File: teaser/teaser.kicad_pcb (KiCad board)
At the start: 2 copper layers, 71 parts, among them J1 Programator, J2 AC_Plug, J3 OLED, J4 battery, Q1 MMBTA44, Q2 MMBTA44, Q3 MMBTA44, Q4 MMBTA44, Q6 AO3401A, SW1 Włancznik, SW2 SW_SPST, SW3 Manual, SW4 Manual, SW5 Manual, SW7 SW_Push, U2 LM1117MP-5.0, U3 ATmega328P-A, Y1 16kHz

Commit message: Most of high voltage routed
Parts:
- moved D7 182.2 mm to (78.8, 128.8), turned to 90 degrees
- moved U3 179.3 mm to (73.0, 83.0)
- moved D4 177.9 mm to (83.0, 128.8), turned to 90 degrees
- moved D5 173.7 mm to (87.2, 128.9), turned to 90 degrees
- moved H4 94.1 mm to (90.0, 177.0)
- moved D2 44.5 mm to (91.5, 128.8), turned to 90 degrees
- moved C12 42.1 mm to (91.0, 139.0), turned to 180 degrees
- moved K4 31.5 mm to (57.4, 138.4)
- moved J2 29.4 mm to (84.0, 61.8)
- moved C11 29.0 mm to (87.0, 168.0), turned to 180 degrees
- moved C8 28.7 mm to (86.5, 150.5), turned to 180 degrees
- moved C7 28.3 mm to (86.0, 159.0), turned to 180 degrees
- moved C10 24.3 mm to (80.0, 176.8), turned to 180 degrees
- moved K2 19.2 mm to (57.4, 155.2)
- moved K3 19.2 mm to (57.4, 172.1)
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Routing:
- net Net-(D4-A): track 0.00 -> 109.7 mm
- net /CH2_230: track 0.00 -> 72.1 mm
- net Net-(D2-K): track 0.00 -> 71.2 mm
- net /CH3_230: track 0.00 -> 53.8 mm
- net Net-(D2-A): track 0.00 -> 43.0 mm
- net /CH1_230: track 0.00 -> 30.2 mm
- added copper zone on F.Cu, net Net-(D2-A)
- added copper zone on F.Cu, net Net-(D2-K)
- added copper zone on F.Cu, net Net-(D4-A)
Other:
- board outline added: 43 x 136 mm

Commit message: Continue routing
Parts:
- D2: footprint Diode_THT:D_DO-41_SOD81_P10.16mm_Horizontal -> Diode_THT:D_DO-41_SOD81_P12.70mm_Horizontal; moved to B.Cu
- moved D13 234.2 mm to (54.0, 171.4), turned to 90 degrees
- moved D12 229.2 mm to (54.0, 154.6), turned to 90 degrees
- moved D14 223.0 mm to (54.0, 137.8), turned to 90 degrees
- moved D15 219.3 mm to (54.0, 121.0), turned to 90 degrees
- moved R15 207.5 mm to (54.0, 167.5), turned to -90 degrees
- moved R14 205.0 mm to (54.0, 150.7), turned to -90 degrees
- moved R11 203.4 mm to (53.2, 90.9), turned to 90 degrees
- moved R17 203.2 mm to (54.0, 117.2), turned to -90 degrees
- moved R16 203.0 mm to (54.0, 134.0), turned to -90 degrees
- moved R10 201.2 mm to (54.9, 90.9), turned to 90 degrees
- moved R9 199.2 mm to (56.5, 90.9), turned to 90 degrees
- moved D1 198.7 mm to (41.5, 76.7)
- moved R8 197.1 mm to (58.2, 90.9), turned to 90 degrees
- moved D3 187.6 mm to (41.9, 81.8)
- moved D6 187.6 mm to (41.9, 86.3)
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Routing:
- net Net-(D2-K): track 71.2 -> 139.1 mm, vias 0 -> 6
- net VCC: track 0.00 -> 64.7 mm
- net Net-(D4-A): track 109.7 -> 162.0 mm
- net Net-(D2-A): track 43.0 -> 6.75 mm
- net /CH3_230: track 53.8 -> 53.0 mm
- removed copper zone on F.Cu, net Net-(D2-A)
- removed copper zone on F.Cu, net Net-(D4-A)

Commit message: Continue routing
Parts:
- D1, D3, D6, D8: moved to B.Cu
- moved D1 41.0 mm to (66.0, 109.5), turned to -90 degrees
- moved D3 34.3 mm to (62.0, 109.5), turned to -90 degrees
- moved D6 28.2 mm to (58.0, 109.5), turned to -90 degrees
- moved D8 22.2 mm to (54.0, 109.5), turned to -90 degrees
- moved R10 9.78 mm to (54.7, 100.7)
- moved R11 9.78 mm to (53.0, 100.7)
- moved R8 9.78 mm to (58.0, 100.7)
- moved R9 9.78 mm to (56.3, 100.7)
- moved Q3 9.61 mm to (53.7, 106.3), turned to -90 degrees
- moved Q4 9.22 mm to (61.7, 100.8), turned to 0 degrees
- moved Q2 9.09 mm to (57.5, 106.3), turned to -90 degrees
- moved Q1 8.50 mm to (61.2, 106.3), turned to -90 degrees
- moved U3 3.61 mm to (64.2, 83.8)
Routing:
- net Net-(D13-K): track 0.00 -> 78.1 mm, vias 0 -> 1
- net VCC: track 64.7 -> 139.5 mm, vias 0 -> 1
- net Net-(D12-K): track 0.00 -> 64.0 mm, vias 0 -> 1
- net Net-(D14-K): track 0.00 -> 60.3 mm, vias 0 -> 1
- net Net-(D1-A): track 0.00 -> 38.8 mm, vias 0 -> 1
- net Net-(Q1-B): track 0.00 -> 8.38 mm
- net /CH1: track 0.00 -> 6.78 mm
- net /CH2: track 0.00 -> 6.71 mm
- net /CH3: track 0.00 -> 6.56 mm
- net /MEASURE_EN: track 0.00 -> 6.51 mm
- net Net-(Q2-B): track 0.00 -> 6.17 mm
- net Net-(Q3-B): track 0.00 -> 4.43 mm
- net Net-(Q4-B): track 0.00 -> 3.47 mm
- net Net-(D12-A): track 0.00 -> 2.12 mm
- net Net-(D13-A): track 0.00 -> 2.10 mm
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
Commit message: Continue routing
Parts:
- C13, C14, D10, D11, D9, R1, R2, R3, R4, R5, R6: moved to B.Cu
- moved Y1 200.4 mm to (55.3, 93.7), turned to 90 degrees
- moved C13 194.4 mm to (57.3, 89.4), turned to 90 degrees
- moved C14 194.2 mm to (57.3, 93.1), turned to -90 degrees
- moved J1 191.7 mm to (57.5, 82.6), turned to 180 degrees
- moved D9 166.5 mm to (98.5, 104.1), turned to 180 degrees
- moved R2 147.3 mm to (104.9, 97.1), turned to 180 degrees
- moved R4 147.3 mm to (104.9, 99.6), turned to 180 degrees
- moved R6 147.3 mm to (104.9, 102.1), turned to 180 degrees
- moved D10 131.0 mm to (98.5, 96.4), turned to 180 degrees
- moved D11 131.0 mm to (98.5, 99.7), turned to 180 degrees
- moved R1 112.2 mm to (109.1, 96.5), turned to 180 degrees
- moved R3 112.2 mm to (109.1, 99.5), turned to 180 degrees
- moved R5 112.2 mm to (109.1, 102.5), turned to 180 degrees
- moved Q4 9.85 mm to (62.1, 110.6), turned to -90 degrees
- moved R10 5.23 mm to (59.9, 101.2)
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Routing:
- net Net-(D2-K): track 139.1 -> 88.8 mm
- net GND: track 0.00 -> 41.4 mm
- net Net-(D4-A): track 162.0 -> 132.7 mm
- net VCC: track 139.5 -> 152.3 mm
- net Net-(U3-XTAL2/PB7): track 0.00 -> 11.0 mm
- net Net-(U3-XTAL1/PB6): track 0.00 -> 9.28 mm
- net Net-(D1-A): track 38.8 -> 30.6 mm
- net /CH1: track 6.78 -> 13.9 mm
- net /CH2: track 6.71 -> 13.4 mm
- net /CH3: track 6.56 -> 13.0 mm
- net /MEASURE_EN: track 6.51 -> 12.3 mm
- net Net-(Q1-B): track 8.38 -> 3.26 mm
- net Net-(Q4-B): track 3.47 -> 7.63 mm
- net Net-(Q2-B): track 6.17 -> 3.59 mm
- net Net-(Q3-B): track 4.43 -> 5.46 mm
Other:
- board text added: "GND"
- board text added: "MI"
- board text added: "MO"
- board text added: "RST"
- board text added: "SCK"
- board text added: "VCC"

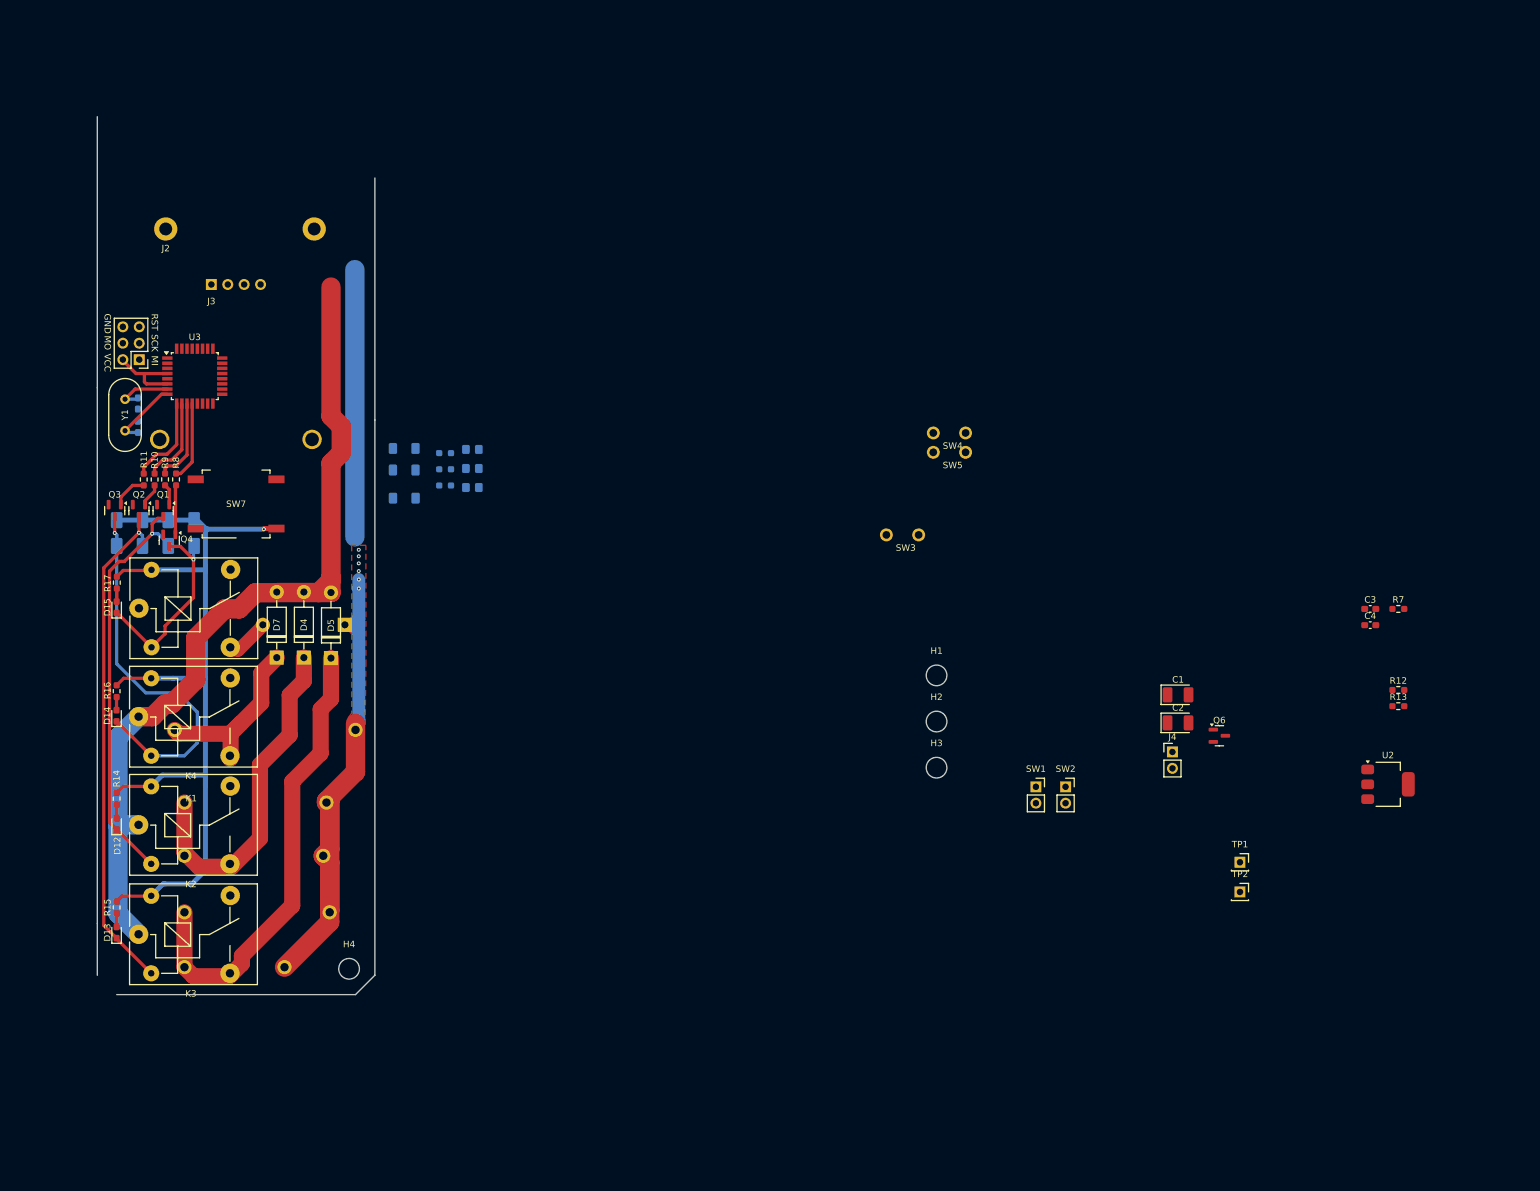
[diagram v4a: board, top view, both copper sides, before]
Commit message: Finalized board outline
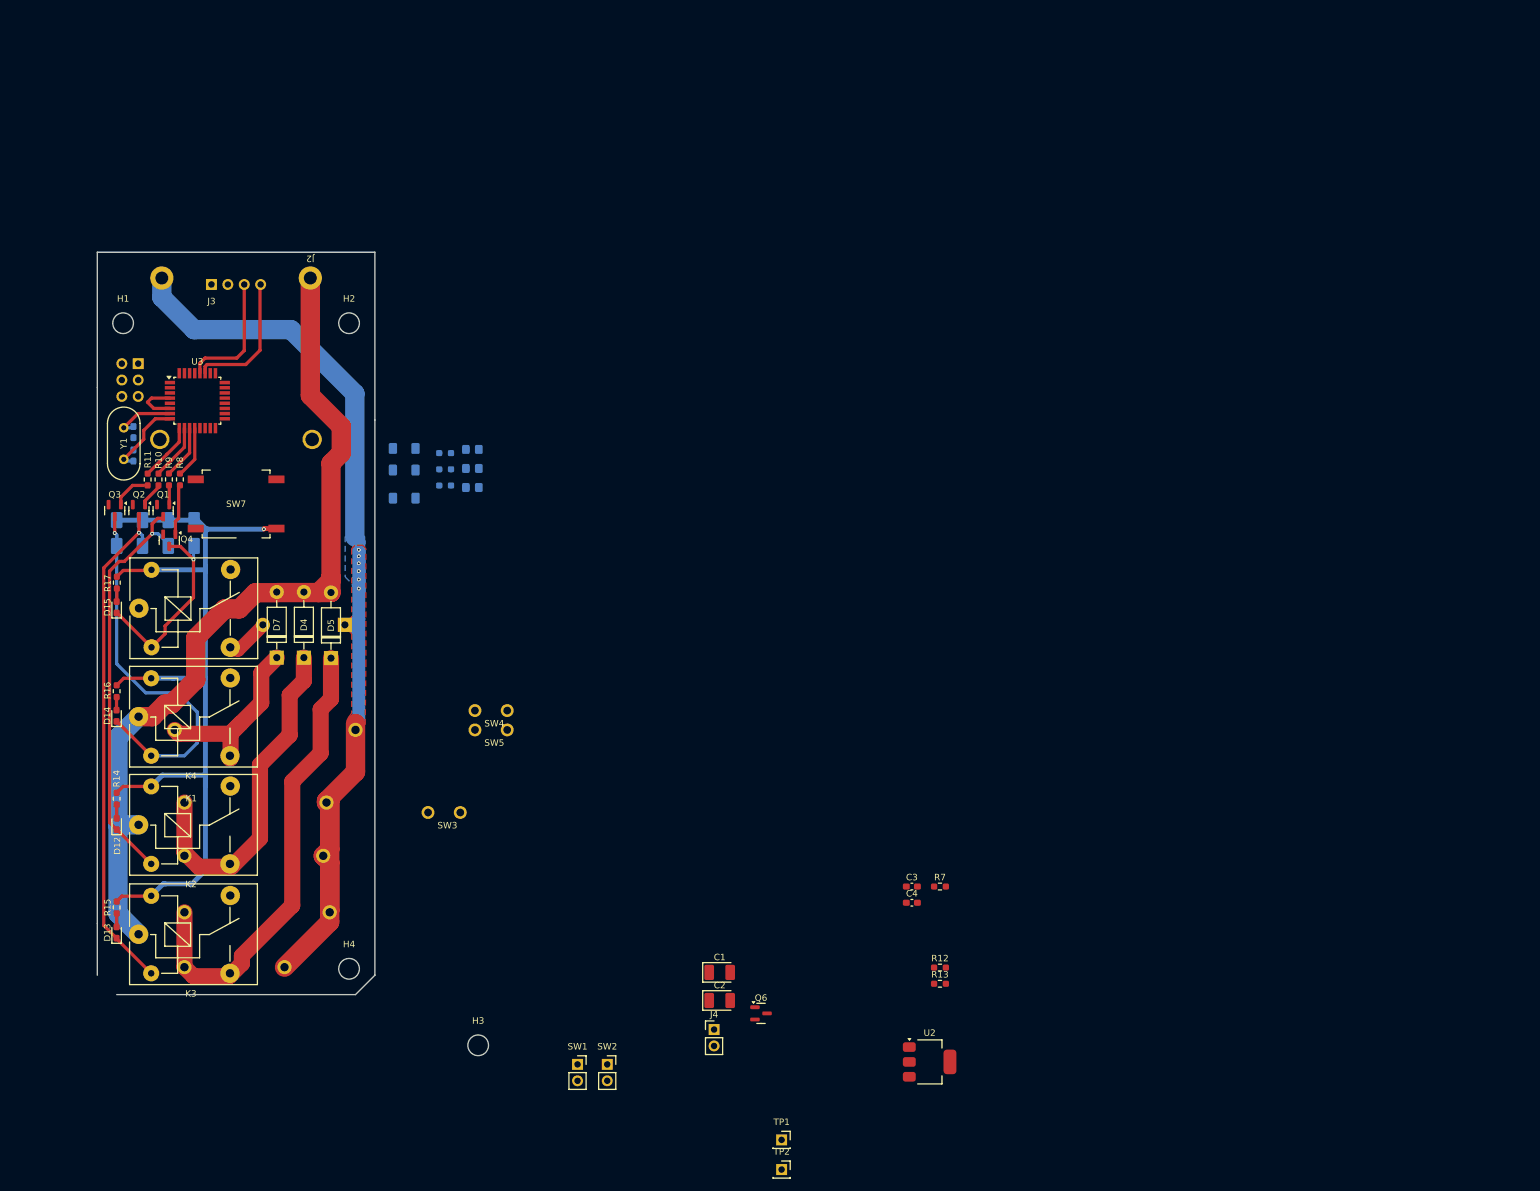
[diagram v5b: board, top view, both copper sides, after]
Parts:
- J1: moved to B.Cu
- moved H1 137.3 mm to (55.0, 77.0)
- moved H2 109.9 mm to (90.0, 77.0)
- moved C4 83.0 mm to (177.2, 166.8)
- moved C1 83.0 mm to (147.4, 177.6)
- moved C2 83.0 mm to (147.4, 181.9)
- moved H3 83.0 mm to (110.0, 188.8)
- moved J4 83.0 mm to (146.5, 186.4)
- moved Q6 83.0 mm to (153.8, 183.9)
- moved R12 83.0 mm to (181.5, 176.8)
- moved R13 83.0 mm to (181.5, 179.3)
- moved SW2 83.0 mm to (130.0, 191.8)
- moved SW4 83.0 mm to (109.5, 137.0)
- moved SW5 83.0 mm to (109.5, 140.0)
- moved TP1 83.0 mm to (157.0, 203.5)
- moved TP2 83.0 mm to (157.0, 208.1)
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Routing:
- net Net-(D2-K): track 88.8 -> 157.0 mm
- net GND: track 41.4 -> 0.00 mm
- net /SDA: track 0.00 -> 20.8 mm
- net /SCL: track 0.00 -> 19.5 mm
- net VCC: track 152.3 -> 147.2 mm
- net /CH1: track 13.9 -> 9.08 mm
- net /CH2: track 13.4 -> 8.72 mm
- net /CH3: track 13.0 -> 8.36 mm
- net /MEASURE_EN: track 12.3 -> 7.94 mm
- net Net-(D4-A): track 132.7 -> 135.4 mm
- net Net-(U3-XTAL2/PB7): track 11.0 -> 12.3 mm
- net Net-(U3-XTAL1/PB6): track 9.28 -> 10.2 mm
- added copper zone on B.Cu, net Net-(D2-K)
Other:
- board size 43 x 136 mm -> 43 x 115 mm
- board text added: "Jak 230 będzie interferowało z I2C to pociągnie się je po kablu nad płytką"

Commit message: Changed layout a little for voltage measuremets
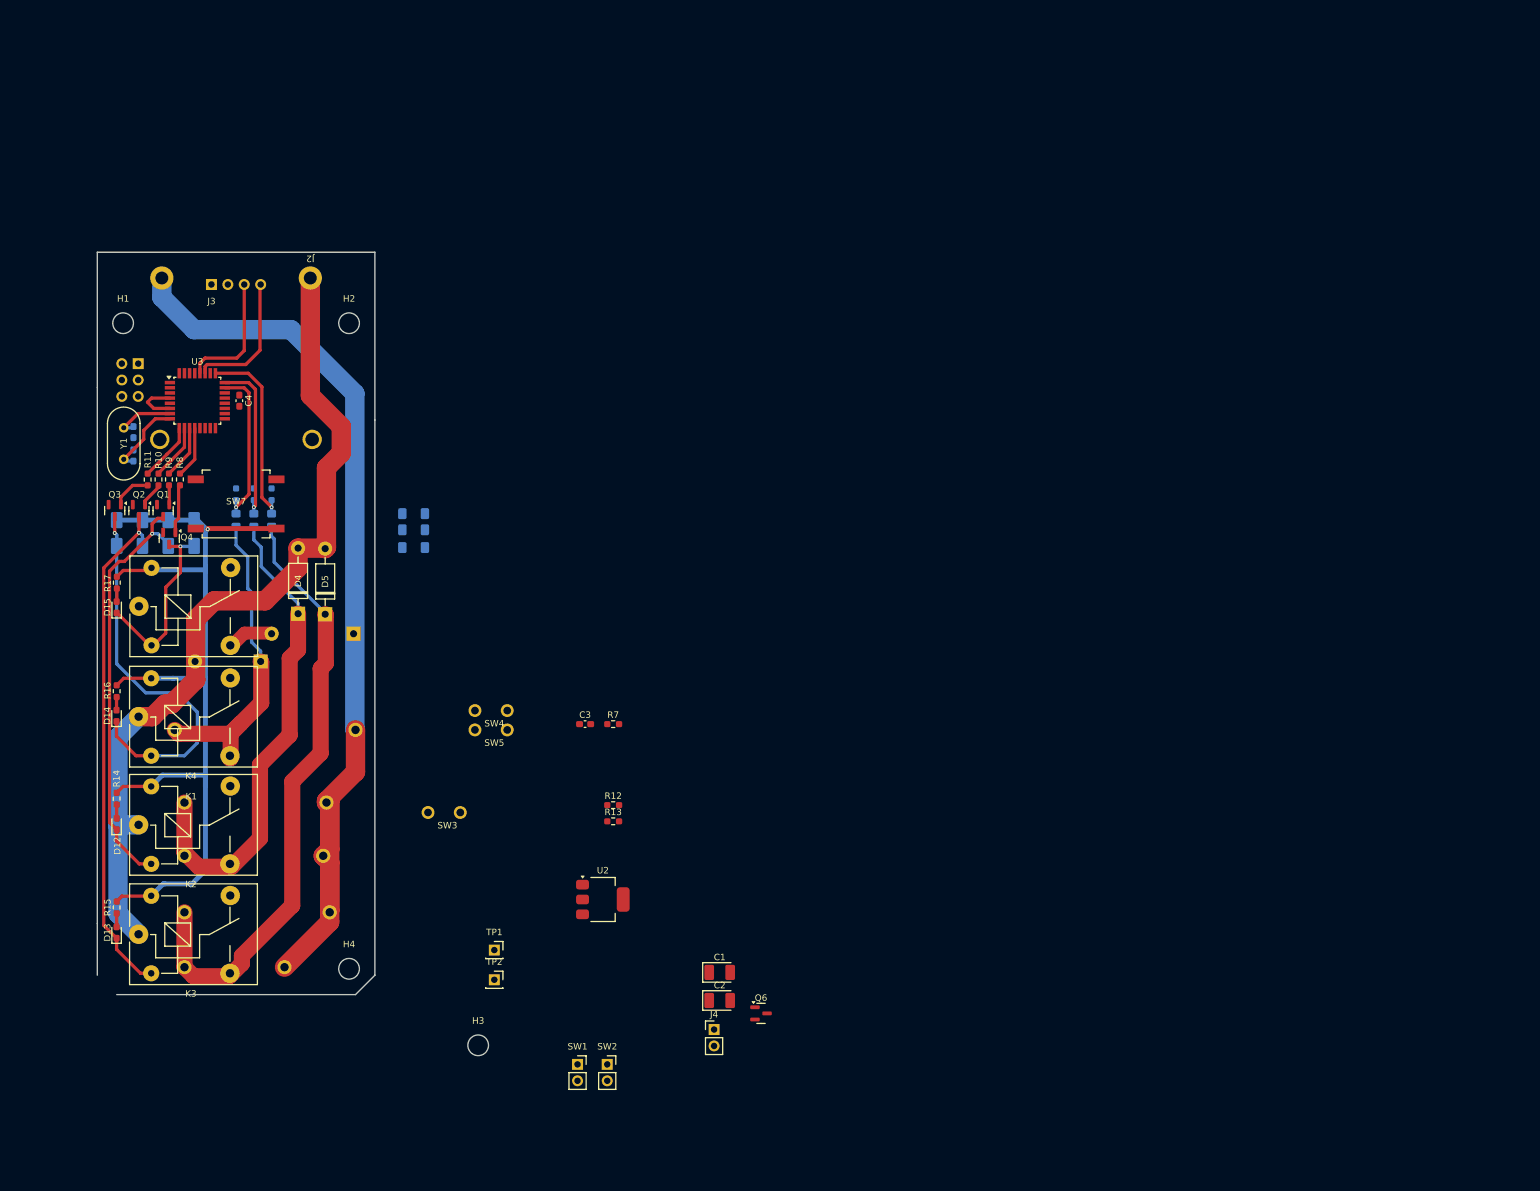
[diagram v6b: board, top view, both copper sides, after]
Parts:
- D7: moved to B.Cu
- moved C4 130.0 mm to (73.0, 89.0), turned to -90 degrees
- moved U2 56.5 mm to (129.3, 166.3)
- moved C3 56.5 mm to (126.6, 139.1)
- moved R12 56.5 mm to (130.9, 151.7)
- moved R13 56.5 mm to (130.9, 154.2)
- moved R7 56.5 mm to (130.9, 139.1)
- moved TP1 53.3 mm to (112.5, 174.1)
- moved TP2 53.3 mm to (112.5, 178.7)
- moved R1 38.2 mm to (72.5, 107.5), turned to 90 degrees
- moved R5 34.2 mm to (75.2, 107.5), turned to 90 degrees
- moved R4 32.6 mm to (72.5, 103.5), turned to 90 degrees
- moved R3 32.1 mm to (78.0, 107.5), turned to 90 degrees
- moved R6 29.7 mm to (75.2, 103.5), turned to 90 degrees
- moved R2 27.6 mm to (78.0, 103.5), turned to 90 degrees
- moved D10 12.7 mm to (100.0, 109.0)
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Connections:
- U3 pad 24: /CH2_MEASURE -> /CH3_MEASURE
- U3 pad 25: /CH3_MEASURE -> /CH2_MEASURE
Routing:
- net /CH2_MEASURE: track 0.00 -> 29.5 mm, vias 0 -> 1
- net /CH3_MEASURE: track 0.00 -> 25.6 mm, vias 0 -> 1
- net /CH1_MEASURE: track 0.00 -> 25.0 mm, vias 0 -> 1
- net /CH2_230: track 71.8 -> 95.1 mm
- net /CH3_230: track 53.0 -> 75.6 mm
- net /CH1_230: track 29.8 -> 50.7 mm
- net Net-(D2-K): track 157.0 -> 152.2 mm, vias 6 -> 0
- net Net-(D4-A): track 135.4 -> 131.6 mm
- net Net-(D1-A): track 30.6 -> 29.0 mm
- net Net-(D14-K): track 60.3 -> 61.7 mm
- net Net-(D12-K): track 64.1 -> 65.1 mm
- net Net-(D13-K): track 78.1 -> 79.1 mm
- net Net-(D2-A): track 6.75 -> 7.36 mm
- removed copper zone on B.Cu, net Net-(D2-K)
- removed copper zone on F.Cu, net Net-(D2-K)

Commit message: Layout near finished
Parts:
- removed TP1: 5V_TP, Connector_PinSocket_2.54mm:PinSocket_1x01_P2.54mm_Vertical
- removed TP2: GND_TP, Connector_PinSocket_2.54mm:PinSocket_1x01_P2.54mm_Vertical
- added C5: 100n, Capacitor_SMD:C_0603_1608Metric_Pad1.08x0.95mm_HandSolder, F.Cu at (73.0, 92.6)
- added C6: 100n, Capacitor_SMD:C_0603_1608Metric_Pad1.08x0.95mm_HandSolder, B.Cu at (60.1, 87.6)
- added C9: 100n, Capacitor_SMD:C_0603_1608Metric_Pad1.08x0.95mm_HandSolder, B.Cu at (64.3, 90.4)
- C1, C2, C3, Q6, R13, R7, U2: moved to B.Cu
- moved J4 124.2 mm to (77.1, 83.4), turned to -90 degrees
- moved Q6 116.0 mm to (73.8, 99.9), turned to -90 degrees
- moved SW1 109.8 mm to (70.5, 96.7), turned to -90 degrees
- moved C2 109.7 mm to (79.1, 96.1)
- moved C1 103.5 mm to (79.1, 99.8)
- moved SW2 100.8 mm to (103.6, 94.5)
- moved R12 99.5 mm to (61.0, 80.9), turned to -90 degrees
- moved U2 92.3 mm to (77.7, 89.8), turned to 90 degrees
- moved C3 82.6 mm to (62.0, 87.6), turned to -90 degrees
- moved R13 82.2 mm to (73.2, 95.7), turned to 90 degrees
- moved R7 81.5 mm to (64.3, 92.1)
- moved D9 30.2 mm to (69.8, 104.9), turned to 90 degrees
- moved D11 26.6 mm to (74.3, 104.9), turned to 90 degrees
- moved D10 21.6 mm to (78.8, 104.9), turned to 90 degrees
- moved R2 3.88 mm to (81.0, 105.9)
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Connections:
- J4 pad 1: Net-(J4-Pin_1) -> GND
- J4 pad 2: GND -> Net-(J4-Pin_2)
- SW1 pad 1: Net-(J4-Pin_1) -> Net-(J4-Pin_2)
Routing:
- net /MOSI: track 0.00 -> 29.8 mm, vias 0 -> 1
- net VCC: track 147.3 -> 174.5 mm, vias 1 -> 3
- net Net-(U3-PD2): track 0.00 -> 26.7 mm, vias 0 -> 2
- net /SCK: track 0.00 -> 21.4 mm, vias 0 -> 1
- net /MISO: track 0.00 -> 19.8 mm, vias 0 -> 1
- net /RESET: track 0.00 -> 15.8 mm
- net /CH1_MEASURE: track 25.0 -> 29.1 mm
- net /CH2_MEASURE: track 29.5 -> 33.5 mm
- net /CH3_MEASURE: track 25.6 -> 29.4 mm
- net /CH1_230: track 50.7 -> 48.3 mm
- net /CH2_230: track 95.1 -> 92.9 mm
- net Net-(U3-AREF): track 0.00 -> 2.04 mm
- net GND: track 0.00 -> 2.04 mm
- net /CH3_230: track 75.6 -> 73.8 mm
- net /SCL: track 19.5 -> 18.7 mm
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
